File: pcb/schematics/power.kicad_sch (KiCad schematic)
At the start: 2 parts

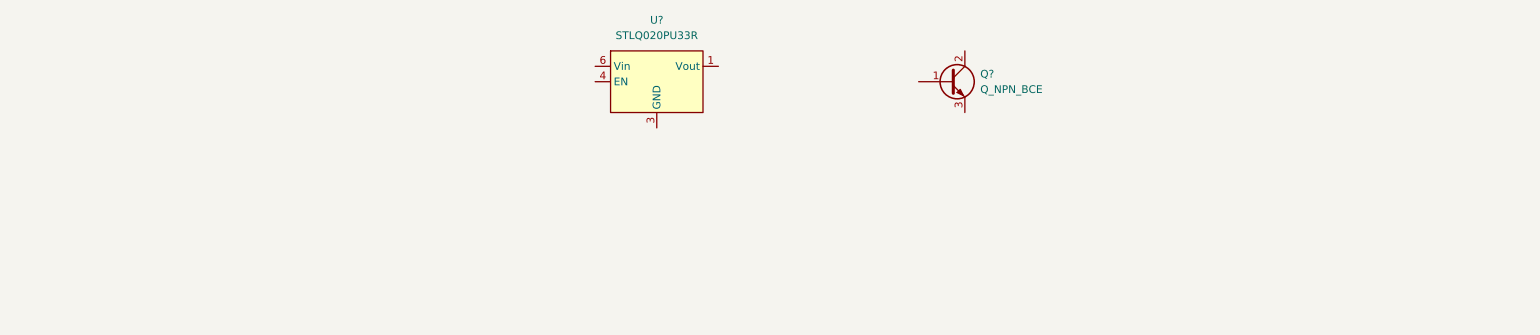
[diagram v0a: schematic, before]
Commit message: add power schematics
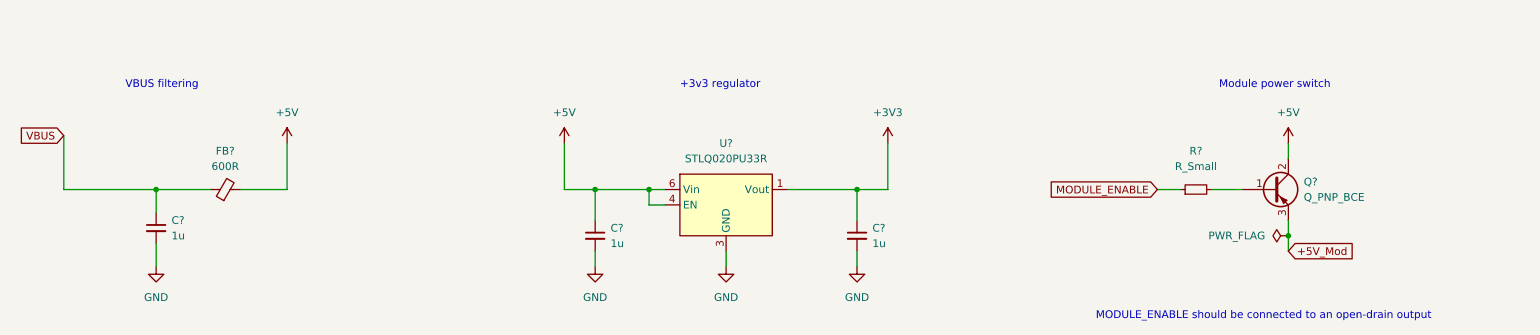
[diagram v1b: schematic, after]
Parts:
- removed Q?: Q_NPN_BCE, symbol Device:Q_NPN_BCE
- added C? (x3): 1u, symbol Device:C_Small
- added FB?: 600R, symbol Device:FerriteBead_Small
- added Q?: Q_PNP_BCE, symbol Device:Q_PNP_BCE
- added R?: R_Small, symbol Device:R_Small
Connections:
- net +3V3: now reaches U?.1 (Vout)
- net +3V3: now also C?.1
- net GND: now reaches U?.3 (GND)
- net GND: now also C?.2, C?.2, C?.2
- net +5V: now reaches U?.4 (EN)
- net +5V: now also U?.6 (Vin), C?.1, FB?.2, Q?.2 (C)
- new net: Q?.1 (B), R?.2
- new net +5V_Mod: Q?.3 (E)
- new net MODULE_ENABLE: R?.1
- new net VBUS: C?.1, FB?.1
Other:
- note added: "+3v3 regulator"
- note added: "MODULE_ENABLE should be connected to an open-drain output"
- note added: "Module power switch"
- note added: "VBUS filtering"
- moved on the sheet: U?

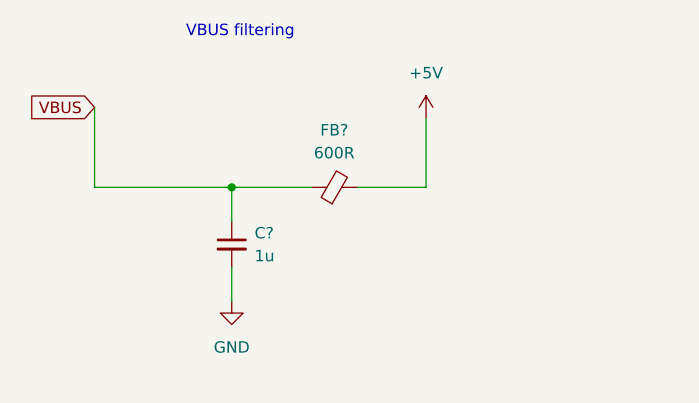
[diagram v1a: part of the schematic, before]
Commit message: start the schematics for the usb to spi interface
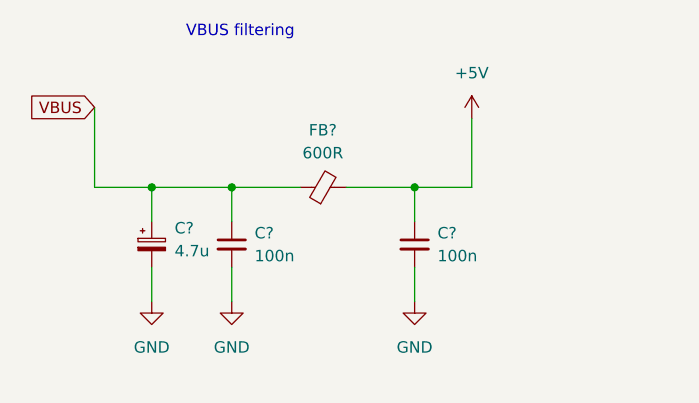
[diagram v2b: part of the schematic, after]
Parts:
- added C?: 4.7u, symbol Device:C_Polarized_Small
- added C?: 100n, symbol Device:C_Small
- C?: value 1u -> 100n
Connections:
- net +5V: now also C?.1
- net GND: now also C?.2, C?.2
- net VBUS: now also C?.1
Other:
- moved on the sheet: FB?
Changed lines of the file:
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@@
 (kicad_sch (version 20211123) (generator eeschema)
   (paper "A4")
+  (junction (at 48.26 90.17) (diameter 0) (color 0 0 0 0)
+  )
   (junction (at 129.54 90.17) (diameter 0) (color 0 0 0 0)
   )
@@
   (junction (at 138.43 90.17) (diameter 0) (color 0 0 0 0)
   )
+  (junction (at 77.47 90.17) (diameter 0) (color 0 0 0 0)
+  )
   (junction (at 243.84 97.79) (diameter 0) (color 0 0 0 0)
   )
@@
     (stroke (width 0) (type default) (color 0 0 0 0))
   )
+  (wire (pts (xy 48.26 99.06) (xy 48.26 102.87))
+    (stroke (width 0) (type default) (color 0 0 0 0))
+  )
   (wire (pts (xy 172.72 100.33) (xy 172.72 102.87))
     (stroke (width 0) (type default) (color 0 0 0 0))
   )
+  (wire (pts (xy 77.47 99.06) (xy 77.47 102.87))
+    (stroke (width 0) (type default) (color 0 0 0 0))
+  )
   (wire (pts (xy 124.46 90.17) (xy 129.54 90.17))
     (stroke (width 0) (type default) (color 0 0 0 0))
   )
-  (wire (pts (xy 71.12 90.17) (xy 78.74 90.17))
-    (stroke (width 0) (type default) (color 0 0 0 0))
-  )
-  (wire (pts (xy 78.74 82.55) (xy 78.74 90.17))
+  (wire (pts (xy 69.85 90.17) (xy 77.47 90.17))
+    (stroke (width 0) (type default) (color 0 0 0 0))
+  )
+  (wire (pts (xy 77.47 90.17) (xy 77.47 93.98))
+    (stroke (width 0) (type default) (color 0 0 0 0))
+  )
+  (wire (pts (xy 83.82 82.55) (xy 83.82 90.17))
     (stroke (width 0) (type default) (color 0 0 0 0))
   )
@@
     (stroke (width 0) (type default) (color 0 0 0 0))
   )
-  (wire (pts (xy 41.91 90.17) (xy 57.15 90.17))
+  (wire (pts (xy 41.91 90.17) (xy 48.26 90.17))
     (stroke (width 0) (type default) (color 0 0 0 0))
   )
@@
     (stroke (width 0) (type default) (color 0 0 0 0))
   )
-  (wire (pts (xy 57.15 90.17) (xy 66.04 90.17))
+  (wire (pts (xy 57.15 90.17) (xy 64.77 90.17))
     (stroke (width 0) (type default) (color 0 0 0 0))
   )
@@
     (stroke (width 0) (type default) (color 0 0 0 0))
   )
+  (wire (pts (xy 77.47 90.17) (xy 83.82 90.17))
+    (stroke (width 0) (type default) (color 0 0 0 0))
+  )
+  (wire (pts (xy 48.26 90.17) (xy 57.15 90.17))
+    (stroke (width 0) (type default) (color 0 0 0 0))
+  )
   (wire (pts (xy 161.29 90.17) (xy 172.72 90.17))
     (stroke (width 0) (type default) (color 0 0 0 0))
@@
   )
   (wire (pts (xy 231.14 90.17) (xy 236.22 90.17))
+    (stroke (width 0) (type default) (color 0 0 0 0))
+  )
+  (wire (pts (xy 48.26 90.17) (xy 48.26 93.98))
     (stroke (width 0) (type default) (color 0 0 0 0))
   )
@@
     )
   )
+  (symbol (lib_id "Device:C_Polarized_Small") (at 48.26 96.52 0) (unit 1)
+    (in_bom yes) (on_board yes) (fields_autoplaced)
+    (property "Reference" "C?" (id 0) (at 50.8 94.7038 0)
+      (effects (font (size 1.27 1.27)) (justify left))
+    )
+    (property "Value" "4.7u" (id 1) (at 50.8 97.2438 0)
+      (effects (font (size 1.27 1.27)) (justify left))
+    )
+    (property "Footprint" "" (id 2) (at 48.26 96.52 0)
+      (effects (font (size 1.27 1.27)) hide)
+    )
+    (property "Datasheet" "~" (id 3) (at 48.26 96.52 0)
+      (effects (font (size 1.27 1.27)) hide)
+    )
+    (pin "1")
+    (pin "2")
+  )
   (symbol (lib_id "power:+3V3") (at 177.8 82.55 0) (unit 1)
     (in_bom yes) (on_board yes) (fields_autoplaced)
@@
     (pin "1")
   )
-  (symbol (lib_id "Device:FerriteBead_Small") (at 68.58 90.17 90) (unit 1)
-    (in_bom yes) (on_board yes) (fields_autoplaced)
-    (property "Reference" "FB?" (id 0) (at 68.5419 83.82 90))
-    (property "Value" "600R" (id 1) (at 68.5419 86.36 90))
-    (property "Footprint" "" (id 2) (at 68.58 91.948 90)
-      (effects (font (size 1.27 1.27)) hide)
-    )
-    (property "Datasheet" "~" (id 3) (at 68.58 90.17 0)
+  (symbol (lib_id "Device:C_Small") (at 77.47 96.52 0) (unit 1)
+    (in_bom yes) (on_board yes)
+    (property "Reference" "C?" (id 0) (at 80.01 95.2562 0)
+      (effects (font (size 1.27 1.27)) (justify left))
+    )
+    (property "Value" "100n" (id 1) (at 80.01 97.7962 0)
+      (effects (font (size 1.27 1.27)) (justify left))
+    )
+    (property "Footprint" "" (id 2) (at 77.47 96.52 0)
+      (effects (font (size 1.27 1.27)) hide)
+    )
+    (property "Datasheet" "~" (id 3) (at 77.47 96.52 0)
       (effects (font (size 1.27 1.27)) hide)
     )
@@
     (pin "2")
   )
-  (symbol (lib_id "power:+5V") (at 78.74 82.55 0) (unit 1)
-    (in_bom yes) (on_board yes) (fields_autoplaced)
-    (property "Reference" "#PWR?" (id 0) (at 78.74 86.36 0)
-      (effects (font (size 1.27 1.27)) hide)
-    )
-    (property "Value" "+5V" (id 1) (at 78.74 77.47 0))
-    (property "Footprint" "" (id 2) (at 78.74 82.55 0)
-      (effects (font (size 1.27 1.27)) hide)
-    )
-    (property "Datasheet" "" (id 3) (at 78.74 82.55 0)
+  (symbol (lib_id "Device:FerriteBead_Small") (at 67.31 90.17 90) (unit 1)
+    (in_bom yes) (on_board yes) (fields_autoplaced)
+    (property "Reference" "FB?" (id 0) (at 67.2719 83.82 90))
+    (property "Value" "600R" (id 1) (at 67.2719 86.36 90))
+    (property "Footprint" "" (id 2) (at 67.31 91.948 90)
+      (effects (font (size 1.27 1.27)) hide)
+    )
+    (property "Datasheet" "~" (id 3) (at 67.31 90.17 0)
+      (effects (font (size 1.27 1.27)) hide)
+    )
+    (pin "1")
+    (pin "2")
+  )
+  (symbol (lib_id "power:+5V") (at 83.82 82.55 0) (unit 1)
+    (in_bom yes) (on_board yes) (fields_autoplaced)
+    (property "Reference" "#PWR?" (id 0) (at 83.82 86.36 0)
+      (effects (font (size 1.27 1.27)) hide)
+    )
+    (property "Value" "+5V" (id 1) (at 83.82 77.47 0))
+    (property "Footprint" "" (id 2) (at 83.82 82.55 0)
+      (effects (font (size 1.27 1.27)) hide)
+    )
+    (property "Datasheet" "" (id 3) (at 83.82 82.55 0)
+      (effects (font (size 1.27 1.27)) hide)
+    )
+    (pin "1")
+  )
+  (symbol (lib_id "power:GND") (at 48.26 102.87 0) (unit 1)
+    (in_bom yes) (on_board yes) (fields_autoplaced)
+    (property "Reference" "#PWR?" (id 0) (at 48.26 109.22 0)
+      (effects (font (size 1.27 1.27)) hide)
+    )
+    (property "Value" "GND" (id 1) (at 48.26 107.95 0))
+    (property "Footprint" "" (id 2) (at 48.26 102.87 0)
+      (effects (font (size 1.27 1.27)) hide)
+    )
+    (property "Datasheet" "" (id 3) (at 48.26 102.87 0)
+      (effects (font (size 1.27 1.27)) hide)
+    )
+    (pin "1")
+  )
+  (symbol (lib_id "power:GND") (at 77.47 102.87 0) (unit 1)
+    (in_bom yes) (on_board yes) (fields_autoplaced)
+    (property "Reference" "#PWR?" (id 0) (at 77.47 109.22 0)
+      (effects (font (size 1.27 1.27)) hide)
+    )
+    (property "Value" "GND" (id 1) (at 77.47 107.95 0))
+    (property "Footprint" "" (id 2) (at 77.47 102.87 0)
+      (effects (font (size 1.27 1.27)) hide)
+    )
+    (property "Datasheet" "" (id 3) (at 77.47 102.87 0)
       (effects (font (size 1.27 1.27)) hide)
     )
@@
   )
   (symbol (lib_id "Device:C_Small") (at 57.15 96.52 0) (unit 1)
-    (in_bom yes) (on_board yes) (fields_autoplaced)
+    (in_bom yes) (on_board yes)
     (property "Reference" "C?" (id 0) (at 59.69 95.2562 0)
       (effects (font (size 1.27 1.27)) (justify left))
     )
-    (property "Value" "1u" (id 1) (at 59.69 97.7962 0)
-      (effects (font (size 1.27 1.27)) (justify left))
-    )
+    (property "Value" "100n" (id 1) (at 59.69 97.7962 0)
+      (effects (font (size 1.27 1.27)) (justify left))
+    )

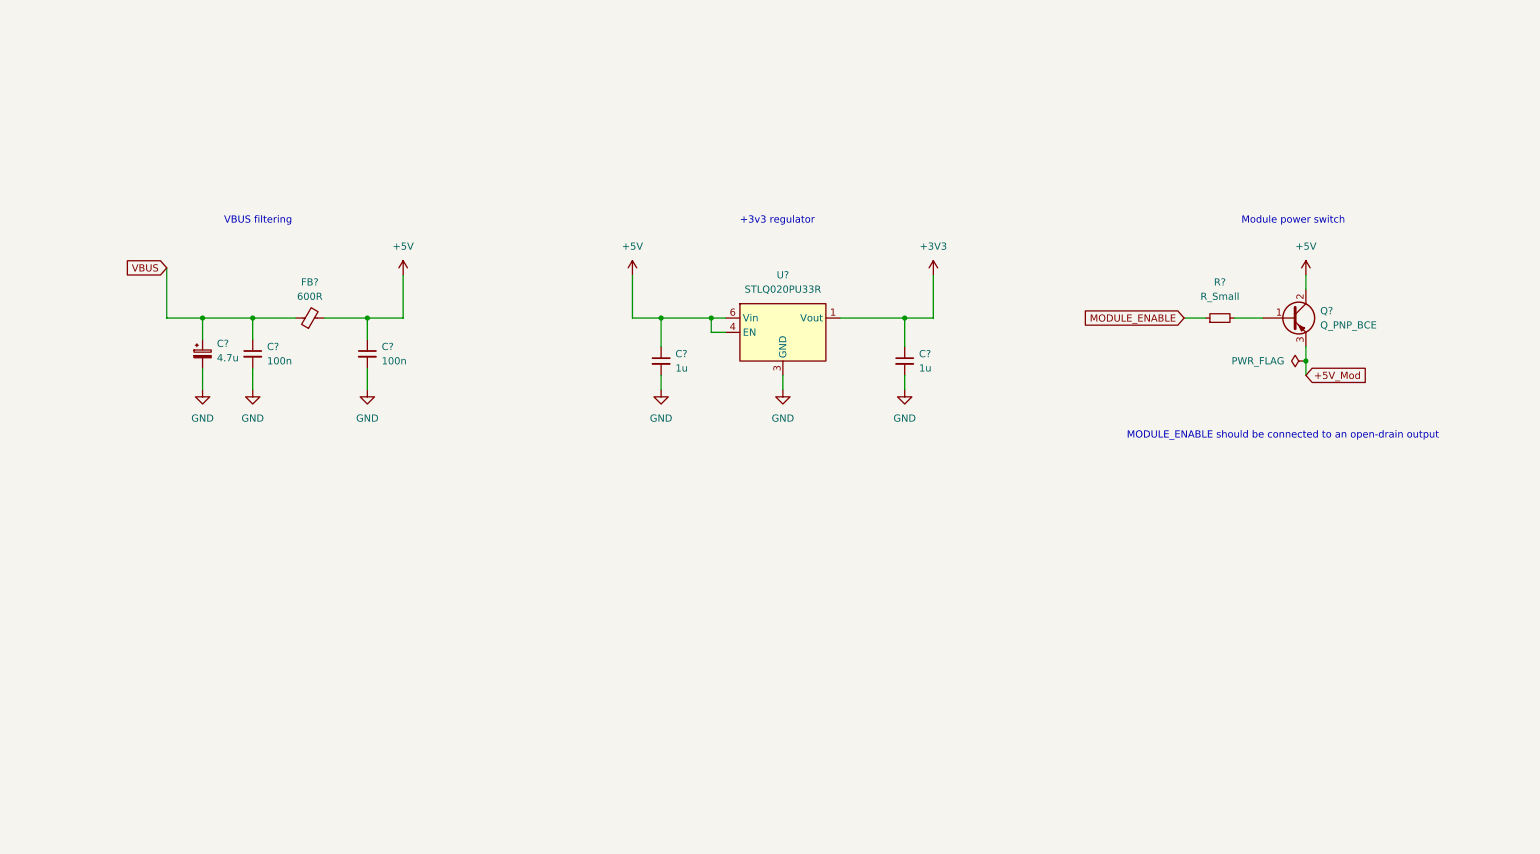
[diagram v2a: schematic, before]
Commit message: start choosing components, need to add overcurren t protection
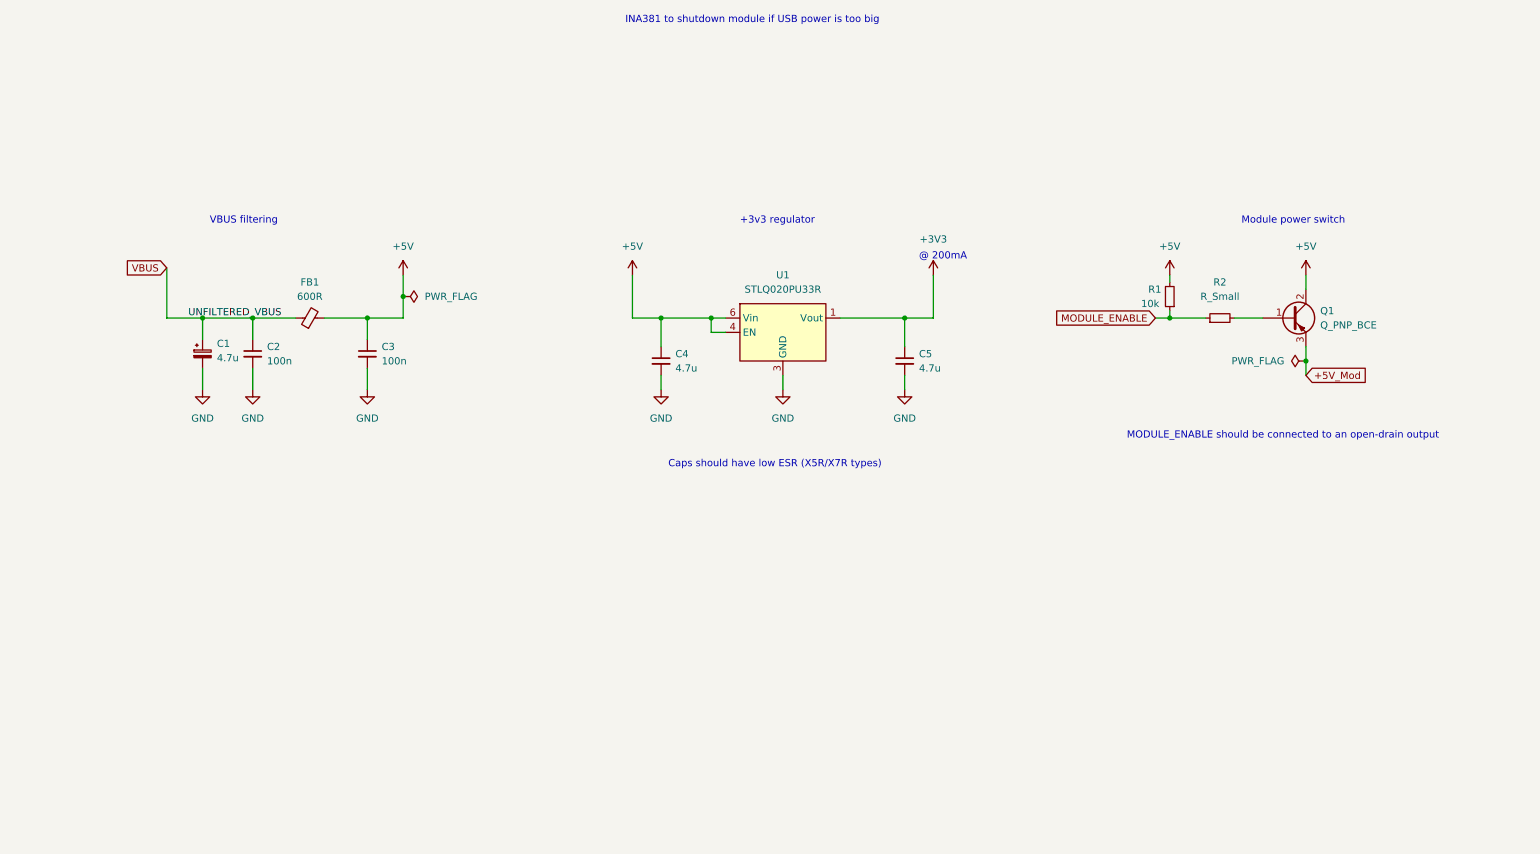
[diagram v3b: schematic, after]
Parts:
- added R1: 10k, symbol Device:R_Small
- C1: renamed from C?; footprint (none) -> Capacitor_SMD:C_0805_2012Metric; Part Number (none) -> GRM21BR71C475KE51L
- C2, C3: renamed from C?; footprint (none) -> Capacitor_SMD:C_0603_1608Metric; Part Number (none) -> 885012206095
- C4, C5: renamed from C?; value 1u -> 4.7u; footprint (none) -> Capacitor_SMD:C_0805_2012Metric; Part Number (none) -> GRM21BR71C475KE51L
- U1: renamed from U?; footprint (none) -> Package_DFN_QFN:DFN-6-1EP_2x2mm_P0.5mm_EP0.6x1.37mm; Part Number (none) -> STLQ020PU33R
- gave numbers to parts that had none: 3
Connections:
- net +5V: now also R1.2
- net MODULE_ENABLE: now also R1.1
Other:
- note added: "@ 200mA"
- note added: "Caps should have low ESR (X5R/X7R types)"
- note added: "INA381 to shutdown module if USB power is too big"

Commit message: add current sensing
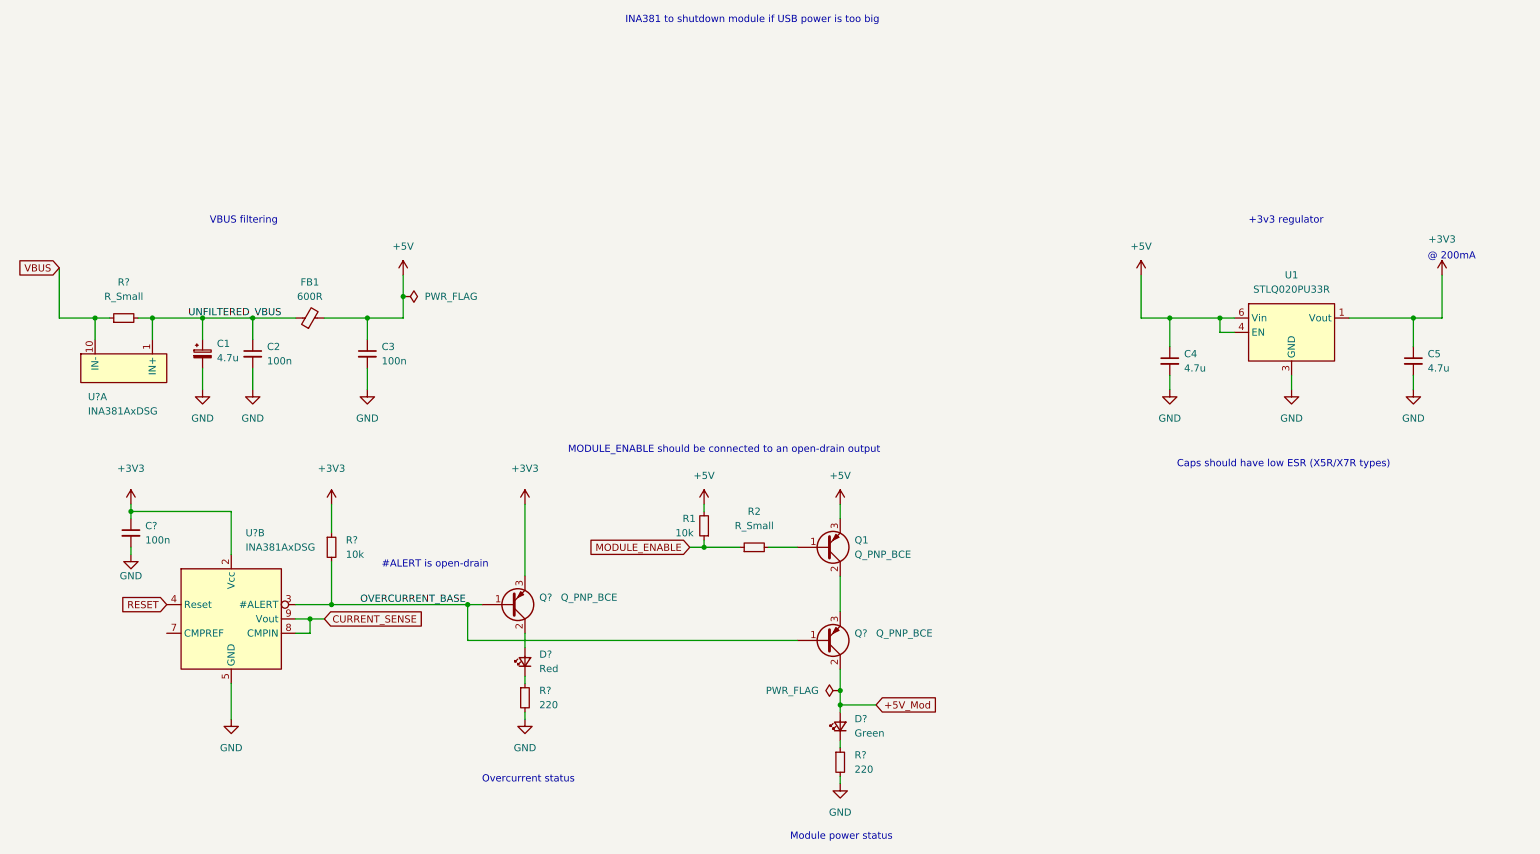
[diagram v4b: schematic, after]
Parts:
- added C?: 100n, Capacitor_SMD:C_0603_1608Metric, symbol Device:C_Small
- added D?: Red, symbol Device:LED_Small
- added D?: Green, symbol Device:LED_Small
- added Q? (x2): Q_PNP_BCE, symbol Device:Q_PNP_BCE
- added R? (x2): 220, symbol Device:R_Small
- added R?: 10k, symbol Device:R_Small
- added R?: R_Small, symbol Device:R_Small
- added U? (x2): INA381AxDSG, symbol INA381:INA381AxDSG
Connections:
- net +3V3: now also C?.1, Q?.3 (E), R?.1, U?.2 (Vcc)
- net +5V: now also Q1.3 (E); no longer Q1.2 (C)
- net +5V_Mod: now also D?.2 (A), Q?.2 (C); no longer Q1.3 (E)
- net GND: now also C?.2, R?.2, R?.2, U?.5 (GND)
- net VBUS: now also R?.1, U?.10 (IN-); no longer C1.1, C2.1, FB1.1
- new net: D?.2 (A), Q?.2 (C)
- new net: D?.1 (K), R?.1 (x2)
- new net: Q1.2 (C), Q?.3 (E)
- new net CURRENT_SENSE: U?.8 (CMPIN), U?.9 (Vout)
- new net OVERCURRENT_BASE: Q?.1 (B), Q?.1 (B), R?.2, U?.3 (#ALERT)
- new net RESET: U?.4 (Reset)
- new net UNFILTERED_VBUS: C1.1, C2.1, FB1.1, R?.2, U?.1 (IN+)
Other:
- note added: "#ALERT is open-drain"
- note added: "Module power status"
- note added: "Overcurrent status"
- note removed: "Module power switch"
- moved on the sheet: C4, C5, Q1, R1, R2, U1
